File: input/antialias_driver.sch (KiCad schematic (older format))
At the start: 16 parts

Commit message: Work on schematics for antialias_driver.sch and in_filter.sch.  Spice simulations of antialias filter and reference driver.
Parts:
- removed C? (x6): 1u, Capacitor_SMD:C_0603_1608Metric, symbol Device:C_Small
- removed J?: Conn_02x02_Odd_Even, symbol Connector_Generic:Conn_02x02_Odd_Even
- removed R? (x3): 499, Resistor_SMD:R_1206_3216Metric, symbol Device:R_US
- removed R?: 49.9, Resistor_SMD:R_0603_1608Metric, symbol Device:R_US
- removed R?: 143, Resistor_SMD:R_0603_1608Metric, symbol Device:R_US
- removed RN?: 1K, Resistor_SMD:R_Array_Convex_4x1206, symbol Device:R_Pack04
- removed U? (x3): LT1028, symbol ilemt_input:opamp_single
- added C? (x6): 1u, Capacitor_SMD:C_0603_1608Metric, symbol Device:C_Small
- added C?: 2.05n, Capacitor_SMD:C_0603_1608Metric, symbol Device:C_Small
- added C?: 16.9n, Capacitor_SMD:C_0603_1608Metric, symbol Device:C_Small
- added R?: 499, Resistor_SMD:R_1206_3216Metric, symbol Device:R_US
- added R?: 750, Resistor_SMD:R_1206_3216Metric, symbol Device:R_US
- added R? (x2): 1.07K, Resistor_SMD:R_1206_3216Metric, symbol Device:R_US
- added R?: 0, Resistor_SMD:R_1206_3216Metric, symbol Device:R_US
- added U? (x3): LT1028, symbol ilemt_input:opamp_single
- added U?: ADA4940-2, Package_CSP:LFCSP-24-1EP_4x4mm_P0.5mm_EP2.5x2.5mm, symbol Amplifier_Difference:ADA4940-2
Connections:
- net labels added: in, ref
- net labels removed: -in
- wire segments 72 -> 54
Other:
- note removed: "Both jumpers: gain 30\nJumper 1-2: gain 21\nJumper 3-4: gain 10\nNo jumpers: gain 3\nNote that ADC driver has gain 1/2, \nso overall gain is half this\n"

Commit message: Continuing work on input board, also added some design files and PDF documentation for the prototype source and sensor.  Deleted various spurious kicad project files.  The main project for the input board is now input_board.pro.
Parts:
- removed C? (x4): 1u, Capacitor_SMD:C_0603_1608Metric, symbol Device:C_Small
- removed R?: 499, Resistor_SMD:R_1206_3216Metric, symbol Device:R_US
- removed U? (x2): LT1028, symbol ilemt_input:opamp_single
- added C117, C120, C123: 1u, Capacitor_SMD:C_0603_1608Metric, symbol Device:C_Small
- added C121, C124: 10.5 nF, Capacitor_SMD:C_0805_2012Metric, symbol Device:C_Small
- added R117, R118: 1K, Resistor_SMD:R_0603_1608Metric, symbol Device:R_US
- added R119, R120: 4.02K, Resistor_SMD:R_0603_1608Metric, symbol Device:R_US
- added R121, R122: 499, Resistor_SMD:R_0603_1608Metric, symbol Device:R_US
- R113, R115, R116: renamed from R?; footprint Resistor_SMD:R_1206_3216Metric -> Resistor_SMD:R_0603_1608Metric
- U106: renamed from U?; value ADA4940-2 -> THS4131; footprint Package_CSP:LFCSP-24-1EP_4x4mm_P0.5mm_EP2.5x2.5mm -> Package_SO:SO-8_5.3x6.2mm_P1.27mm; symbol Amplifier_Difference:ADA4940-2 -> ilemt_input:THS4131
- gave numbers to parts that had none: 6
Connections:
- net labels added: +out, -out, VREF
- net labels removed: +in, out, out_ref
- wire segments 54 -> 82
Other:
- note added: "This is a third-order Butterworth lowpass filter\nand a gain 1/2 single-ended to differential converter.\nThe VOCM also gives a level shift from the zero \nvolt ground reference to the ADC midpoint VREF/2"
- moved on the sheet: C116, C118, C119, C122, R113, R114, R115, R116, U105

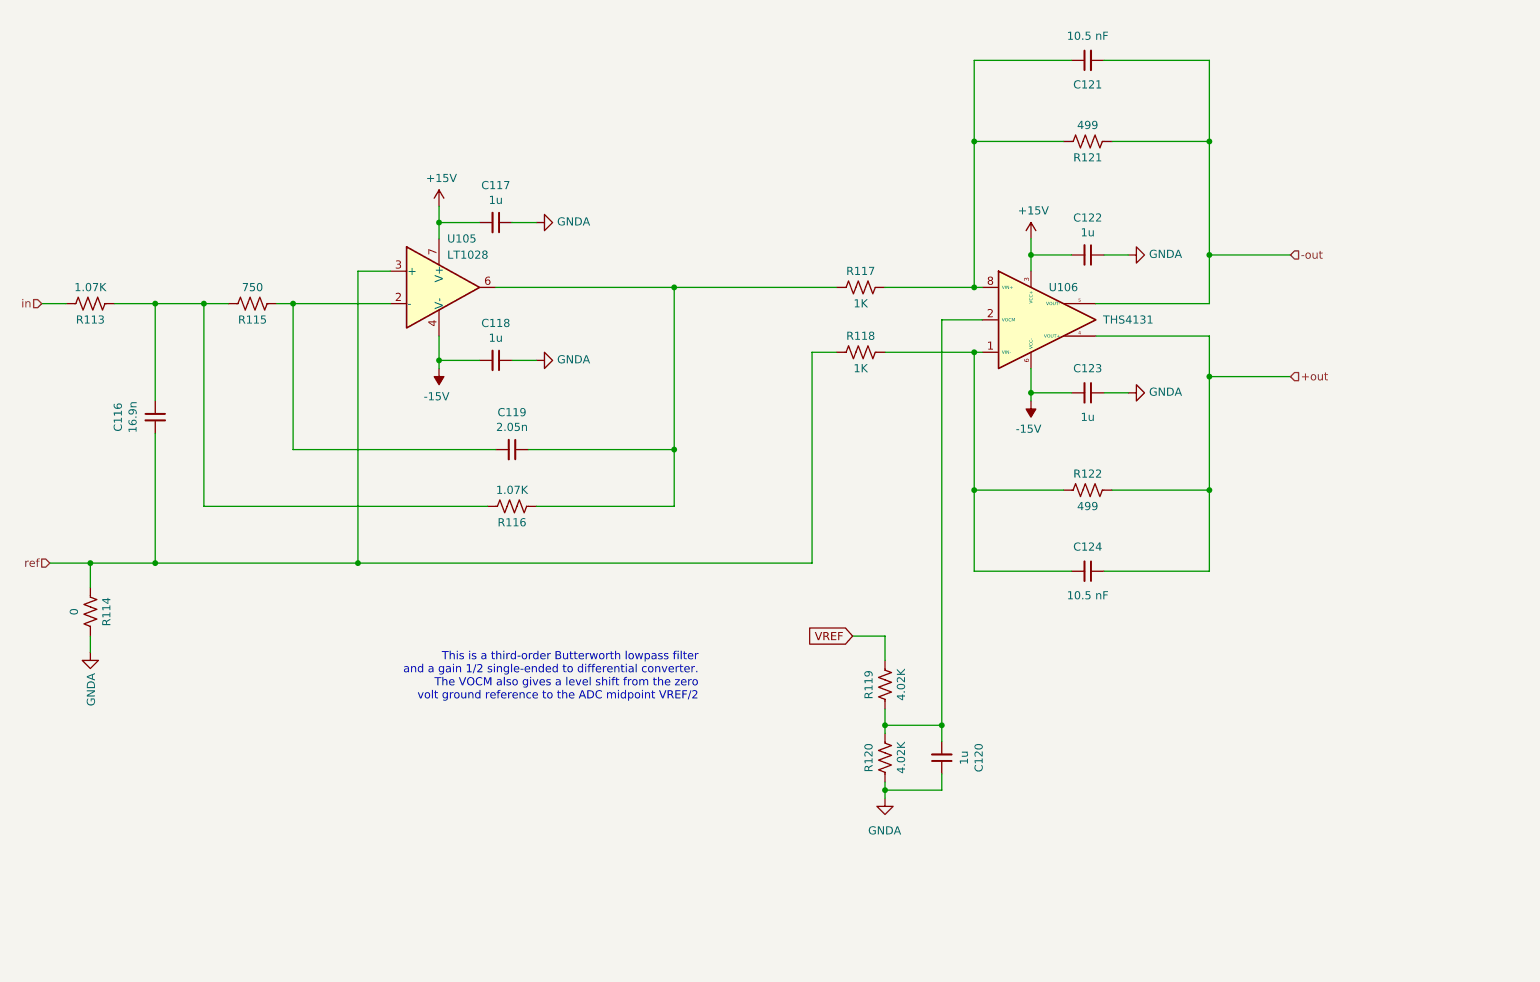
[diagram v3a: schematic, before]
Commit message: Mainly work on the top level of the input board, attaching signals to the channels, digital I/O.  Decided to use Eurocard 64 pin type B connector for the connection to the main board.  See input_board_pinout.txt.
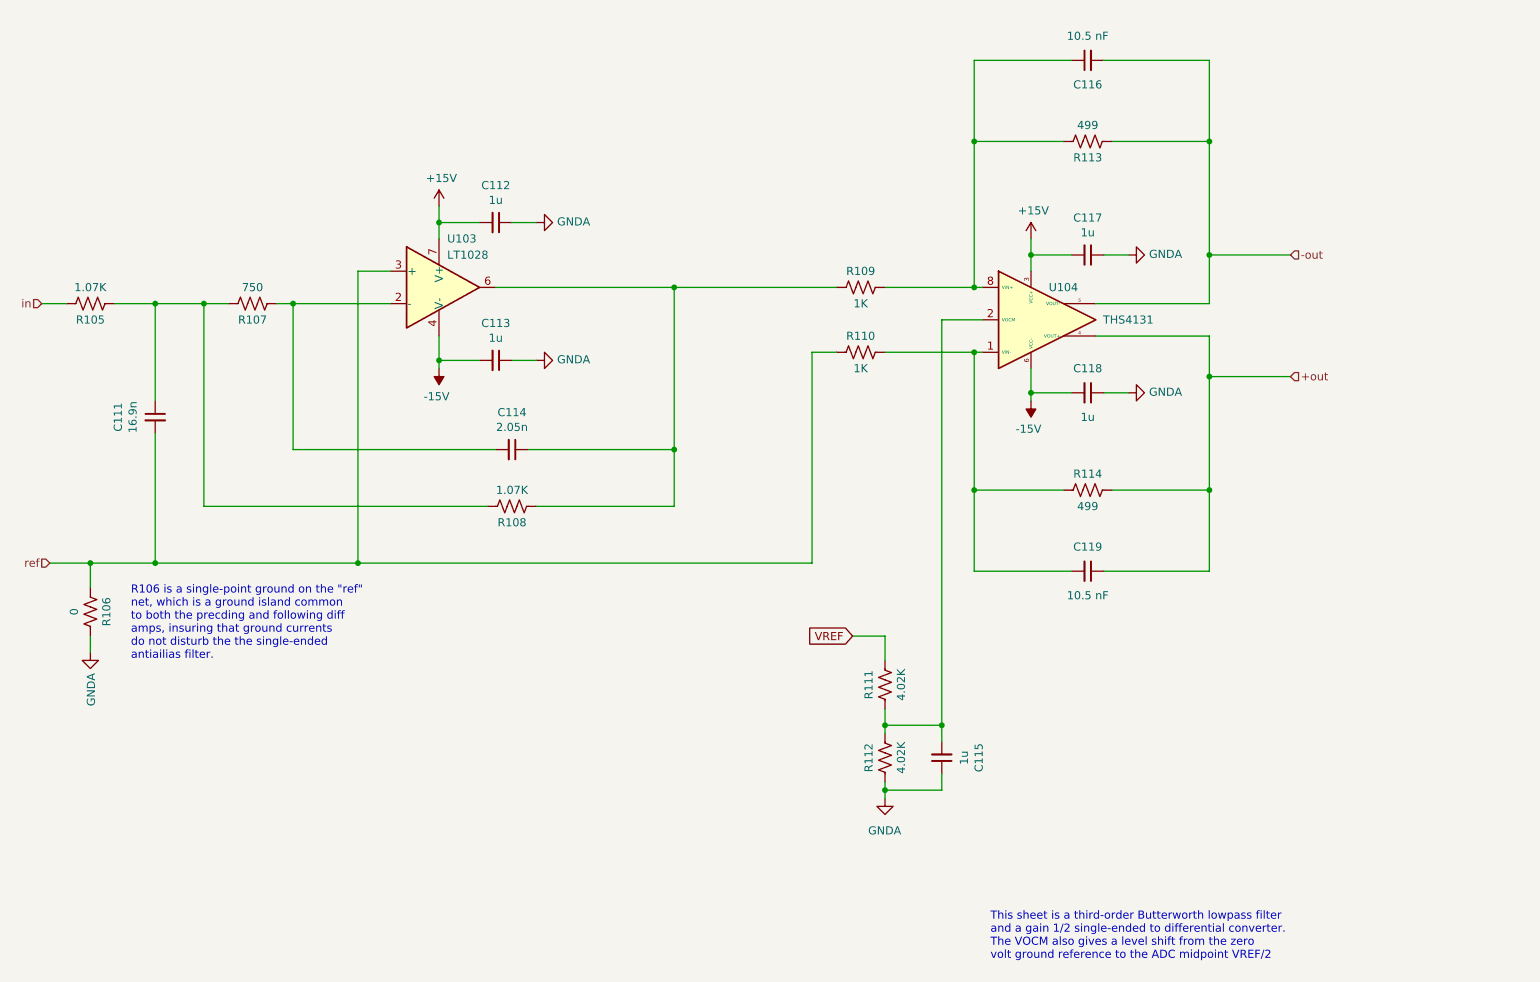
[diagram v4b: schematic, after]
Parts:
- removed C119: 2.05n, Capacitor_SMD:C_0603_1608Metric, symbol Device:C_Small
- removed C120, C122, C123: 1u, Capacitor_SMD:C_0603_1608Metric, symbol Device:C_Small
- removed C121: 10.5 nF, Capacitor_SMD:C_0805_2012Metric, symbol Device:C_Small
- removed R114: 0, Resistor_SMD:R_1206_3216Metric, symbol Device:R_US
- removed R117, R118: 1K, Resistor_SMD:R_0603_1608Metric, symbol Device:R_US
- removed R119, R120: 4.02K, Resistor_SMD:R_0603_1608Metric, symbol Device:R_US
- removed R121: 499, Resistor_SMD:R_0603_1608Metric, symbol Device:R_US
- removed U106: THS4131, Package_SO:SO-8_5.3x6.2mm_P1.27mm, symbol ilemt_input:THS4131
- added C114: 2.05n, Capacitor_SMD:C_0603_1608Metric, symbol Device:C_Small
- added C115, C117, C118: 1u, Capacitor_SMD:C_0603_1608Metric, symbol Device:C_Small
- added C116: 10.5 nF, Capacitor_SMD:C_0805_2012Metric, symbol Device:C_Small
- added R105: 1.07K, Resistor_SMD:R_0603_1608Metric, symbol Device:R_US
- added R106: 0, Resistor_SMD:R_1206_3216Metric, symbol Device:R_US
- added R109, R110: 1K, Resistor_SMD:R_0603_1608Metric, symbol Device:R_US
- added R111, R112: 4.02K, Resistor_SMD:R_0603_1608Metric, symbol Device:R_US
- added U104: THS4131, Package_SO:SO-8_5.3x6.2mm_P1.27mm, symbol ilemt_input:THS4131
- R113: value 1.07K -> 499
- renumbered C116 to C111, C117 to C112, C118 to C113, C124 to C119, R115 to R107, R116 to R108, R122 to R114, U105 to U103
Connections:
- net +15V: now also C117.2, U104.3 (VCC+)
- net +out: now also U104.4 (VOUT+)
- net -15V: now also C118.2, U104.6 (VCC-)
- net -out: now also R113.1, C116.2, U104.5 (VOUT-)
- net GNDA: now also C115.1, C117.1, C118.1, R106.2, R112.1
- net VREF: now also R111.2
- net in: now also R105.2; no longer R113.2
- net ref: now also R106.1, R110.1
- net at R107.1, U103.2 (-): now also C114.2
- net at R108.1, U103.6: now also C114.1, R109.1
- net at C111.1, R107.2, R108.2: now also R105.1; no longer R113.1
- net at C119.2, R114.1: now also R110.2, U104.1 (VIN-)
- new net: C115.2, R111.1, R112.2, U104.2 (VOCM)
- new net: C116.1, R109.2, R113.2, U104.8 (VIN+)
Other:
- note added: "R106 is a single-point ground on the "ref" \nnet, which is a ground island common\nto both the precding and following diff\namps, insuring that ground currents\ndo not disturb the the single-ended\nantiailias filter."
- note added: "This sheet is a third-order Butterworth lowpass filter\nand a gain 1/2 single-ended to differential converter.\nThe VOCM also gives a level shift from the zero \nvolt ground reference to the ADC midpoint VREF/2"
- note removed: "This is a third-order Butterworth lowpass filter\nand a gain 1/2 single-ended to differential converter.\nThe VOCM also gives a level shift from the zero \nvolt ground reference to the ADC midpoint VREF/2"
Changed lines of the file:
@@
 EESchema Schematic File Version 4
+LIBS:input_board-cache
 LIBS:input_channel-cache
 EELAYER 29 0
@@
 $Descr A4 11693 8268
 encoding utf-8
-Sheet 3 5
+Sheet 4 10
 Title ""
 Date ""
@@
 $EndDescr
 $Comp
-L power:+15V #PWR0134
+L power:+15V #PWR0121
 U 1 1 5DE6EE06
 P 7350 2500
-F 0 "#PWR0134" H 7350 2350 50  0001 C CNN
+F 0 "#PWR0121" H 7350 2350 50  0001 C CNN
 F 1 "+15V" H 7365 2673 50  0000 C CNN
 F 2 "" H 7350 2500 50  0001 C CNN
@@
 	7350 2500 7350 2600
 $Comp
-L Device:C_Small C122
-U 1 1 5DE48FEB
+L Device:C_Small C117
+U 1 1 5E195560
 P 7700 2600
-F 0 "C122" V 7471 2600 50  0000 C CNN
+F 0 "C117" V 7471 2600 50  0000 C CNN
 F 1 "1u" V 7562 2600 50  0000 C CNN
 F 2 "Capacitor_SMD:C_0603_1608Metric" H 7700 2600 50  0001 C CNN
@@
 	3700 3100 3700 3250
 $Comp
-L power:-15V #PWR0130
-U 1 1 5DE467A9
+L power:-15V #PWR0117
+U 1 1 5E19555D
 P 3700 3300
-F 0 "#PWR0130" H 3700 3400 50  0001 C CNN
+F 0 "#PWR0117" H 3700 3400 50  0001 C CNN
 F 1 "-15V" H 3715 3473 50  0000 C CNN
 F 2 "" H 3700 3300 50  0001 C CNN
@@
 	7350 2600 7350 2700
 $Comp
-L power:GNDA #PWR0136
+L power:GNDA #PWR0123
 U 1 1 5DE52F1A
 P 7950 2600
-F 0 "#PWR0136" H 7950 2350 50  0001 C CNN
+F 0 "#PWR0123" H 7950 2350 50  0001 C CNN
 F 1 "GNDA" V 7955 2472 50  0000 R CNN
 F 2 "" H 7950 2600 50  0001 C CNN
@@
 	7800 2600 7950 2600
 $Comp
-L Device:C_Small C118
+L Device:C_Small C113
 U 1 1 5DE5507D
 P 4050 3250
-F 0 "C118" V 3821 3250 50  0000 C CNN
+F 0 "C113" V 3821 3250 50  0000 C CNN
 F 1 "1u" V 3912 3250 50  0000 C CNN
 F 2 "Capacitor_SMD:C_0603_1608Metric" H 4050 3250 50  0001 C CNN
@@
 $EndComp
 $Comp
-L power:GNDA #PWR0132
+L power:GNDA #PWR0119
 U 1 1 5DE55083
 P 4300 3250
-F 0 "#PWR0132" H 4300 3000 50  0001 C CNN
+F 0 "#PWR0119" H 4300 3000 50  0001 C CNN
 F 1 "GNDA" V 4305 3122 50  0000 R CNN
 F 2 "" H 4300 3250 50  0001 C CNN
@@
 	4150 3250 4300 3250
 $Comp
-L ilemt_input:opamp_single U105
+L ilemt_input:opamp_single U103
 U 1 1 5DE6EE05
 P 3650 2800
-F 0 "U105" H 3750 3100 50  0000 L CNN
+F 0 "U103" H 3750 3100 50  0000 L CNN
 F 1 "LT1028" H 3750 3000 50  0000 L CNN
 F 2 "" H 3700 2850 50  0001 C CNN
@@
 	3700 3250 3950 3250
 $Comp
-L Device:R_US R115
+L Device:R_US R107
 U 1 1 5DE6EE13
 P 2550 2900
-F 0 "R115" V 2650 2900 50  0000 C CNN
+F 0 "R107" V 2650 2900 50  0000 C CNN
 F 1 "750" V 2450 2900 50  0000 C CNN
 F 2 "Resistor_SMD:R_0603_1608Metric" V 2590 2890 50  0001 C CNN
@@
 ref
 $Comp
-L Device:R_US R116
+L Device:R_US R108
 U 1 1 5DE73C3F
 P 4150 4150
-F 0 "R116" V 4250 4150 50  0000 C CNN
+F 0 "R108" V 4250 4150 50  0000 C CNN
 F 1 "1.07K" V 4050 4150 50  0000 C CNN
 F 2 "Resistor_SMD:R_0603_1608Metric" V 4190 4140 50  0001 C CNN
@@
 $EndComp
 $Comp
-L Device:C_Small C119
-U 1 1 5DE74D95
+L Device:C_Small C114
+U 1 1 5E195597
 P 4150 3800
-F 0 "C119" V 3921 3800 50  0000 C CNN
+F 0 "C114" V 3921 3800 50  0000 C CNN
 F 1 "2.05n" V 4012 3800 50  0000 C CNN
 F 2 "Capacitor_SMD:C_0603_1608Metric" H 4150 3800 50  0001 C CNN
@@
 $EndComp
 $Comp
-L Device:C_Small C116
+L Device:C_Small C111
 U 1 1 5DE7579B
 P 1950 3600
-F 0 "C116" V 1721 3600 50  0000 C CNN
+F 0 "C111" V 1721 3600 50  0000 C CNN
 F 1 "16.9n" V 1812 3600 50  0000 C CNN
 F 2 "Capacitor_SMD:C_0603_1608Metric" H 1950 3600 50  0001 C CNN
@@
 	2250 2900 2400 2900
 $Comp
-L Device:R_US R113
-U 1 1 5DE7F15D
+L Device:R_US R105
+U 1 1 5E19559A
 P 1550 2900
-F 0 "R113" V 1650 2900 50  0000 C CNN
+F 0 "R105" V 1650 2900 50  0000 C CNN
 F 1 "1.07K" V 1450 2900 50  0000 C CNN
 F 2 "Resistor_SMD:R_0603_1608Metric" V 1590 2890 50  0001 C CNN
@@
 	1300 4500 1550 4500
 $Comp
-L Device:R_US R114
-U 1 1 5DE86C70
+L Device:R_US R106
+U 1 1 5E19559C
 P 1550 4800
-F 0 "R114" V 1650 4800 50  0000 C CNN
+F 0 "R106" V 1650 4800 50  0000 C CNN
 F 1 "0" V 1450 4800 50  0000 C CNN
 F 2 "Resistor_SMD:R_1206_3216Metric" V 1590 4790 50  0001 C CNN
@@
 Connection ~ 1950 4500
 $Comp
-L power:GNDA #PWR0128
-U 1 1 5DE8AB8D
+L power:GNDA #PWR0115
+U 1 1 5E19559F
 P 1550 5050
-F 0 "#PWR0128" H 1550 4800 50  0001 C CNN
+F 0 "#PWR0115" H 1550 4800 50  0001 C CNN
 F 1 "GNDA" V 1555 4922 50  0000 R CNN
 F 2 "" H 1550 5050 50  0001 C CNN
@@
 	1950 4500 1950 3700
 $Comp
-L ilemt_input:THS4131 U106
-U 1 1 5DEA3186
+L ilemt_input:THS4131 U104
+U 1 1 5E1955AA
 P 7350 3000
-F 0 "U106" H 7550 3200 50  0000 C CNN
+F 0 "U104" H 7550 3200 50  0000 C CNN
 F 1 "THS4131" H 7950 3000 50  0000 C CNN
 F 2 "Package_SO:SO-8_5.3x6.2mm_P1.27mm" H 7350 2600 50  0001 C CNN
@@
 	2800 2900 2800 3800
 $Comp
-L Device:R_US R119
-U 1 1 5DEACC57
+L Device:R_US R111
+U 1 1 5E1955AB
 P 6450 5250
-F 0 "R119" V 6550 5250 50  0000 C CNN
+F 0 "R111" V 6550 5250 50  0000 C CNN
 F 1 "4.02K" V 6350 5250 50  0000 C CNN
 F 2 "Resistor_SMD:R_0603_1608Metric" V 6490 5240 50  0001 C CNN
@@
 $EndComp
 $Comp
-L Device:R_US R120
-U 1 1 5DEAF5FA
+L Device:R_US R112
+U 1 1 5E1955AC
 P 6450 5700
-F 0 "R120" V 6550 5700 50  0000 C CNN
+F 0 "R112" V 6550 5700 50  0000 C CNN
 F 1 "4.02K" V 6350 5700 50  0000 C CNN
 F 2 "Resistor_SMD:R_0603_1608Metric" V 6490 5690 50  0001 C CNN
@@
 $EndComp
 $Comp
-L power:GNDA #PWR0133
-U 1 1 5DEB0282
+L power:GNDA #PWR0120
+U 1 1 5E1955AD
 P 6450 5950
-F 0 "#PWR0133" H 6450 5700 50  0001 C CNN
+F 0 "#PWR0120" H 6450 5700 50  0001 C CNN
 F 1 "GNDA" H 6550 5750 50  0000 R CNN
 F 2 "" H 6450 5950 50  0001 C CNN
@@
 	6450 5500 6450 5550
 $Comp
-L Device:C_Small C120
-U 1 1 5DEB23BC
+L Device:C_Small C115
+U 1 1 5E1955AE
 P 6800 5700
-F 0 "C120" V 6571 5700 50  0000 C CNN
+F 0 "C115" V 6571 5700 50  0000 C CNN
 F 1 "1u" V 6662 5700 50  0000 C CNN
 F 2 "Capacitor_SMD:C_0603_1608Metric" H 6800 5700 50  0001 C CNN
@@
 	6450 5900 6450 5950
 $Comp
-L Device:R_US R122
+L Device:R_US R114
 U 1 1 5DEC0082
 P 7700 4050
-F 0 "R122" V 7800 4050 50  0000 C CNN
+F 0 "R114" V 7800 4050 50  0000 C CNN
 F 1 "499" V 7600 4050 50  0000 C CNN
 F 2 "Resistor_SMD:R_0603_1608Metric" V 7740 4040 50  0001 C CNN
@@
 	7000 4050 7550 4050
 $Comp
-L power:+15V #PWR0129
+L power:+15V #PWR0116
 U 1 1 5DED3BAE
 P 3700 2300
-F 0 "#PWR0129" H 3700 2150 50  0001 C CNN
+F 0 "#PWR0116" H 3700 2150 50  0001 C CNN
 F 1 "+15V" H 3715 2473 50  0000 C CNN
 F 2 "" H 3700 2300 50  0001 C CNN
@@
 	3700 2300 3700 2400
 $Comp
-L Device:C_Small C117
+L Device:C_Small C112
 U 1 1 5DED3BB5
 P 4050 2400
-F 0 "C117" V 3821 2400 50  0000 C CNN
+F 0 "C112" V 3821 2400 50  0000 C CNN
 F 1 "1u" V 3912 2400 50  0000 C CNN
 F 2 "Capacitor_SMD:C_0603_1608Metric" H 4050 2400 50  0001 C CNN
@@
 	3700 2400 3700 2500
 $Comp
-L power:GNDA #PWR0131
-U 1 1 5DED3BBE
+L power:GNDA #PWR0118
+U 1 1 5E1955B2
 P 4300 2400
-F 0 "#PWR0131" H 4300 2150 50  0001 C CNN
+F 0 "#PWR0118" H 4300 2150 50  0001 C CNN
 F 1 "GNDA" V 4305 2272 50  0000 R CNN
 F 2 "" H 4300 2400 50  0001 C CNN
@@
 	7350 3300 7350 3450
 $Comp
-L power:-15V #PWR0135
-U 1 1 5DED53EE
+L power:-15V #PWR0122
+U 1 1 5E1955B3
 P 7350 3500
-F 0 "#PWR0135" H 7350 3600 50  0001 C CNN
+F 0 "#PWR0122" H 7350 3600 50  0001 C CNN
 F 1 "-15V" H 7365 3673 50  0000 C CNN
 F 2 "" H 7350 3500 50  0001 C CNN
@@
 $EndComp
 $Comp
-L Device:C_Small C123
-U 1 1 5DED53F4
+L Device:C_Small C118
+U 1 1 5E1955B4
 P 7700 3450
-F 0 "C123" V 7550 3450 50  0000 C CNN
+F 0 "C118" V 7550 3450 50  0000 C CNN
 F 1 "1u" V 7850 3450 50  0000 C CNN
 F 2 "Capacitor_SMD:C_0603_1608Metric" H 7700 3450 50  0001 C CNN
@@
 $EndComp
 $Comp
-L power:GNDA #PWR0137
-U 1 1 5DED53FA
+L power:GNDA #PWR0124
+U 1 1 5E1955B5
 P 7950 3450
-F 0 "#PWR0137" H 7950 3200 50  0001 C CNN
+F 0 "#PWR0124" H 7950 3200 50  0001 C CNN
 F 1 "GNDA" V 7955 3322 50  0000 R CNN
 F 2 "" H 7950 3450 50  0001 C CNN
@@
 	7750 2900 8450 2900
 $Comp
-L Device:R_US R117
-U 1 1 5DEE6EE1
+L Device:R_US R109
+U 1 1 5E1955B6
 P 6300 2800
-F 0 "R117" V 6400 2800 50  0000 C CNN
+F 0 "R109" V 6400 2800 50  0000 C CNN
 F 1 "1K" V 6200 2800 50  0000 C CNN
 F 2 "Resistor_SMD:R_0603_1608Metric" V 6340 2790 50  0001 C CNN
@@
 $EndComp
 $Comp
-L Device:R_US R118
-U 1 1 5DEE7D4E
+L Device:R_US R110
+U 1 1 5E1955B7
 P 6300 3200
-F 0 "R118" V 6400 3200 50  0000 C CNN
+F 0 "R110" V 6400 3200 50  0000 C CNN
 F 1 "1K" V 6200 3200 50  0000 C CNN
 F 2 "Resistor_SMD:R_0603_1608Metric" V 6340 3190 50  0001 C CNN
@@
 Connection ~ 3200 4500
 $Comp
-L Device:C_Small C124
+L Device:C_Small C119
 U 1 1 5DF0AA68
 P 7700 4550
-F 0 "C124" V 7550 4550 50  0000 C CNN
+F 0 "C119" V 7550 4550 50  0000 C CNN
 F 1 "10.5 nF" V 7850 4550 50  0000 C CNN
 F 2 "Capacitor_SMD:C_0805_2012Metric" H 7700 4550 50  0001 C CNN
@@
 	7800 4550 8450 4550
 $Comp
-L Device:R_US R121
-U 1 1 5DF22628
+L Device:R_US R113
+U 1 1 5E1955BB
 P 7700 1900
-F 0 "R121" V 7800 1900 50  0000 C CNN
+F 0 "R113" V 7800 1900 50  0000 C CNN
 F 1 "499" V 7600 1900 50  0000 C CNN
 F 2 "Resistor_SMD:R_0603_1608Metric" V 7740 1890 50  0001 C CNN
@@
 	8450 1900 7850 1900
 $Comp
-L Device:C_Small C121
-U 1 1 5DF22631
+L Device:C_Small C116
+U 1 1 5E1955BC
 P 7700 1400
-F 0 "C121" V 7550 1400 50  0000 C CNN
+F 0 "C116" V 7550 1400 50  0000 C CNN
 F 1 "10.5 nF" V 7850 1400 50  0000 C CNN
 F 2 "Capacitor_SMD:C_0805_2012Metric" H 7700 1400 50  0001 C CNN
@@
 Wire Wire Line
 	6800 3000 7050 3000
-Text Notes 5300 5350 2    50   ~ 0
-This is a third-order Butterworth lowpass filter\nand a gain 1/2 single-ended to differential converter.\nThe VOCM also gives a level shift from the zero \nvolt ground reference to the ADC midpoint VREF/2
+Text Notes 7100 6950 0    50   ~ 0
+This sheet is a third-order Butterworth lowpass filter\nand a gain 1/2 single-ended to differential converter.\nThe VOCM also gives a level shift from the zero \nvolt ground reference to the ADC midpoint VREF/2
+Text Notes 1800 5100 0    50   ~ 0
+R106 is a single-point ground on the "ref" \nnet, which is a ground island common\nto both the precding and following diff\namps, insuring that ground currents\ndo not disturb the the single-ended\nantiailias filter.
 $EndSCHEMATC
